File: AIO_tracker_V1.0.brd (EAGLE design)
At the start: 47 x 95 mm, 57 parts, among them J1 EDGE_ICSP, Q1 MOSFET-PCHANNELSMD, U2 USD-SOCKETNEW, X1 SMA-142-0701-881/886, Y2 16MHz

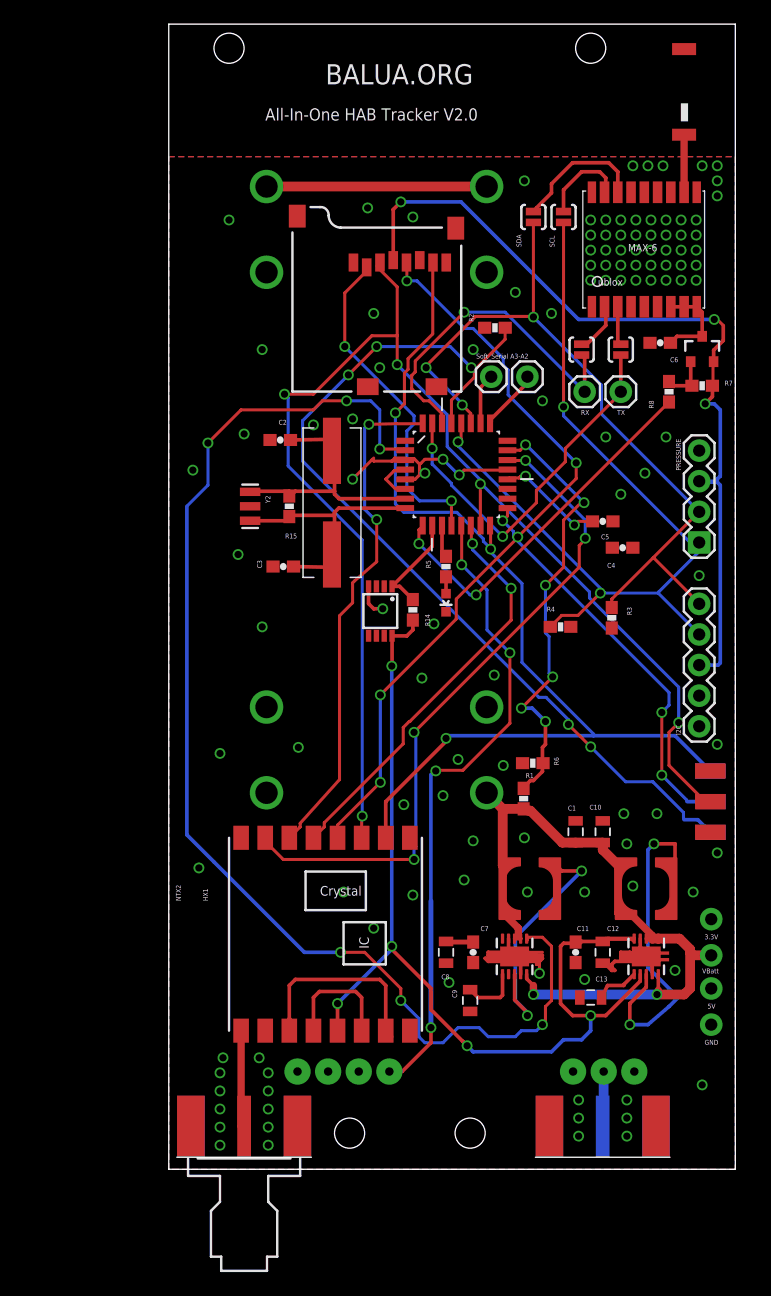
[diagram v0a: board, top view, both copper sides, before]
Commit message: added 9dof, new antena, new crystal, cutoff...
added 9dof, new antena, new crystal, cutoff system and changed layout
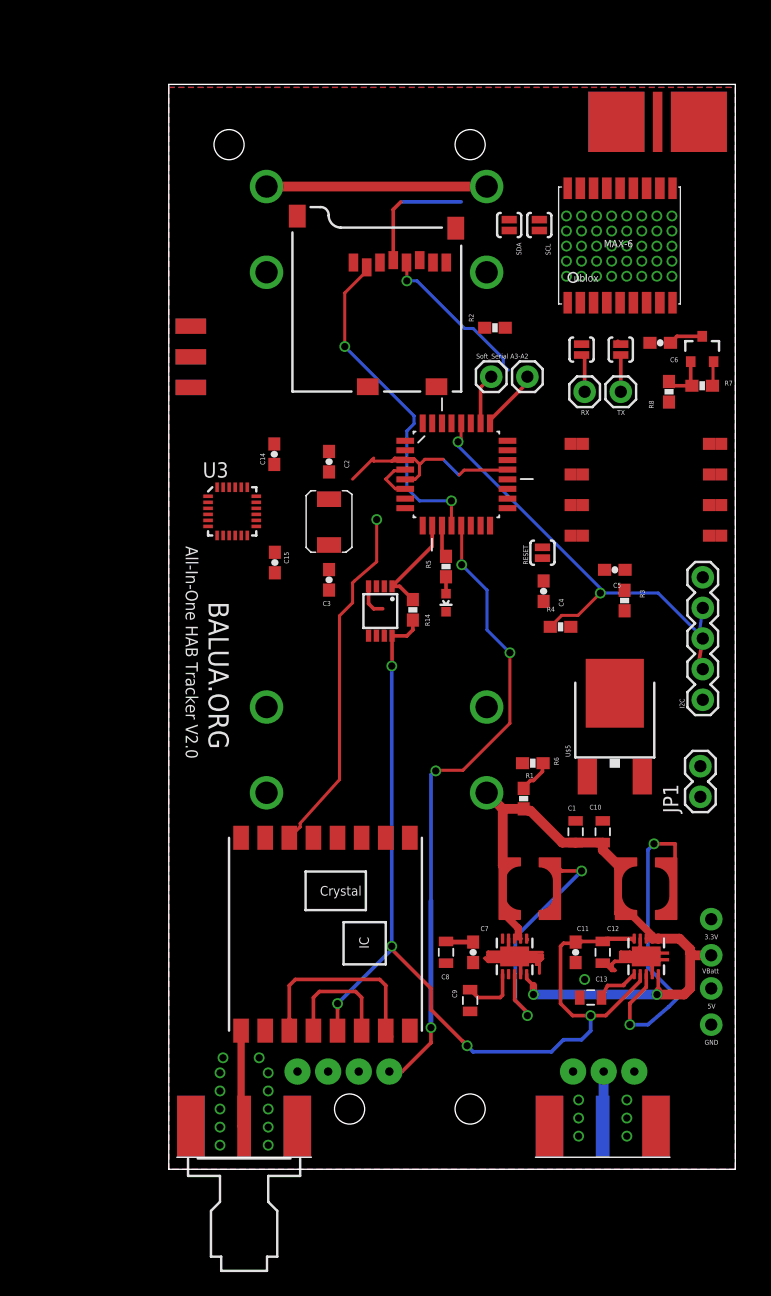
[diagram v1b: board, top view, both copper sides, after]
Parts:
- removed PRESSURE: (no value), SparkFun-Connectors:1X04
- removed R15: 1M, SparkFun-Passives:0603-RES
- removed Y2: 16MHz, SparkFun-FreqCtrl:RESONATOR-SMD
- added C14: 2.2nF, SparkFun-Passives:0603-CAP
- added C15: 0.1uF, SparkFun-Passives:0603-CAP
- added JP1: M02PTH, SparkFun-Connectors:1X02
- added SJ2: SOLDERJUMPERNO, SparkFun-Passives:SJ_2S-NO
- added TP1, TP10, TP11, TP12, TP13, TP14, TP15, TP16, TP2, TP3, TP4, TP5, TP6, TP7, TP8, TP9: TPTP10SQ, testpad:TP10SQ
- added U$5: LM2931_FIXED, SparkFun-PowerIC:DPAK
- added U3: (no value), SparkFun-Sensors:QFN-24-NP
- C2, C3: value 22pF -> 18pF
- U$2: value JTI_ANTENNA-1575AT43A40 -> JDGA-REMQV-ANTENNA; device Ava:JTI_ANTENNA-1575AT43A40 -> Ava:JDGA-RIGID_COMBO_PAD
- Y1: value (none) -> ABRACON_ABM3_CRYSTAL; device SparkFun-FreqCtrl:CRYSTAL-SMD-10.5X4.8-2PIN -> Ava:ABRACON_ABM3_CRYSTAL
- moved J1 56.7 mm to (0.83, 50.4)
- moved C4 7.48 mm to (30.1, 31.0), turned to 270 degrees
- moved C2 4.43 mm to (12.3, 41.7), turned to 270 degrees
- moved C5 4.14 mm to (36.0, 32.7)
- moved C3 3.96 mm to (12.3, 31.9), turned to 90 degrees
- moved U$2 3.04 mm to (39.6, 69.9), turned to 180 degrees
- moved I2C 2.22 mm to (43.3, 21.9)
- moved SJ1 2.12 mm to (27.2, 61.3)
- moved SJ3 2.12 mm to (29.7, 61.3)
- moved U$1 2.04 mm to (36.5, 59.8)
- moved R3 1.78 mm to (36.8, 30.2)
- moved Y1 0.18 mm to (12.4, 38.2)
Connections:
- removed net MARK: U1.24
- removed net SPACE: U1.19
- new net A6: U$7.15, U1.19
- new net CUTOUT: JP1.2, U$5.4
- new net GATE: U$5.1, U1.24
- new net N$14: TP13.TP, TP14.TP
- new net N$17: C15.1, U3.10
- new net N$18: C14.1, U3.20
- new net N$25: TP10.TP, TP11.TP, TP12.TP, TP9.TP
- new net N$8: C4.1, SJ2.1
- new net N$9: TP15.TP, TP16.TP
- net 3.3V: now also SJ2.2, TP3.TP, TP4.TP, U3.13, U3.3, U3.8; no longer C4.1, PRESSURE.3
- net A7: no longer U$7.15
- net GND: now also C14.2, C15.2, JP1.1, TP1.TP, TP2.TP, U$2.P$2, U$2.P$3, U$2.P$4, U$2.P$5, U3.1, U3.11, U3.15, U3.17, U3.18, U3.9; no longer PRESSURE.4, Y2.2
- net N$20: no longer R15.1, Y2.3
- net N$21: no longer R15.2, Y2.1
- net N$3: now also U$2.P$1; no longer U$2.FEED
- net SCL: now also TP7.TP, TP8.TP, U3.23; no longer PRESSURE.1
- net SDA: now also TP5.TP, TP6.TP, U3.24; no longer PRESSURE.2
- net VBATT: now also U$5.3
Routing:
- net MOSI: track 111.6 -> 0.00 mm, vias 5 -> 0
- net EN_POW_5V: track 103.9 -> 0.16 mm, vias 6 -> 0
- net MISO: track 85.4 -> 0.00 mm, vias 3 -> 0
- net SCK: track 96.2 -> 13.3 mm, vias 8 -> 1
- net RESET: track 77.8 -> 0.00 mm, vias 5 -> 0
- net SDA: track 63.0 -> 0.00 mm, vias 3 -> 0
- net 3.3V: track 162.8 -> 106.4 mm, vias 8 -> 5
- net A7: track 56.1 -> 0.00 mm, vias 4 -> 0
- net SCL: track 71.9 -> 36.5 mm, vias 3 -> 2
- net VBATTADC: track 37.3 -> 2.90 mm, vias 6 -> 0
- net RFM22_NSEL: track 34.1 -> 0.00 mm, vias 2 -> 0
- net GPSEN: track 30.8 -> 0.00 mm, vias 2 -> 0
- net UBLOX_RXD: track 30.9 -> 3.05 mm, vias 2 -> 0
- net UBLOX_TXD: track 28.2 -> 3.15 mm, vias 1 -> 0
- net N$21: track 21.8 -> 0.00 mm
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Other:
- board size 47 x 95 mm -> 47 x 90 mm
- board text added: "RESET"
- board text removed: "HX1"
- board text removed: "NTX2"

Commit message: size and placement defined
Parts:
- removed JP1: M02PTH, SparkFun-Connectors:1X02
- removed SJ2: SOLDERJUMPERNO, SparkFun-Passives:SJ_2S-NO
- added CUTOFF: M02PTH, SparkFun-Connectors:1X02
- 3.3V, 5V, GND, VBATT: value M01SMDNS -> M01PTH; device SparkFun-Connectors:1X01NS -> SparkFun-Connectors:1X01
- U$3: value RADIOMETRIX-HX1 -> NTX2-VERTICAL; device Ava:RADIOMETRIX-HX1 -> Ava:NTX2-VERTICAL
- moved TP12 49.2 mm to (-2.53, 29.9), flipped to the bottom, turned to 180 degrees
- moved TP16 48.1 mm to (-2.53, 32.5), flipped to the bottom, turned to 180 degrees
- moved TP9 47.5 mm to (-2.53, 35.0), flipped to the bottom, turned to 180 degrees
- moved TP13 47.4 mm to (-2.53, 37.5), flipped to the bottom, turned to 180 degrees
- moved TP11 47.2 mm to (-1.51, 29.9), flipped to the bottom, turned to 180 degrees
- moved TP15 46.1 mm to (-1.51, 32.5), flipped to the bottom, turned to 180 degrees
- moved TP10 45.4 mm to (-1.51, 35.0), flipped to the bottom, turned to 180 degrees
- moved TP14 45.4 mm to (-1.51, 37.5), flipped to the bottom, turned to 180 degrees
- moved BAT1 36.1 mm to (15.2, 4.77), turned to 0 degrees
- moved R2 33.8 mm to (-1.84, 33.7)
- moved SJ3 29.3 mm to (15.0, 36.0)
- moved U$2 29.1 mm to (36.0, 41.0)
- moved U2 28.6 mm to (5.96, 24.7)
- moved C6 28.5 mm to (38.1, 23.1), turned to 0 degrees
- moved U$1 28.3 mm to (32.9, 31.7)
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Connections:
- removed net N$8: C4.1, SJ2.1
- net 3.3V: now also C4.1; no longer SJ2.2
- net CUTOUT: now also CUTOFF.2; no longer JP1.2
- net GND: now also CUTOFF.1, U$3.RFGND1; no longer JP1.1, U$3.RFGND
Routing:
- net 3.3V: track 106.4 -> 0.00 mm, vias 5 -> 0
- net 5VEN: track 54.0 -> 0.00 mm, vias 4 -> 0
- net VBATT: track 59.8 -> 7.33 mm, vias 2 -> 0
- net GND: track 53.7 -> 1.41 mm, vias 59 -> 56
- net SCL: track 36.5 -> 0.00 mm, vias 2 -> 0
- net RFM22_NIRQ: track 29.5 -> 0.00 mm, vias 1 -> 0
- net SD_CS: track 27.9 -> 0.00 mm, vias 2 -> 0
- net N$19: track 27.9 -> 0.00 mm, vias 2 -> 0
- net N$7: track 20.8 -> 0.00 mm, vias 2 -> 0
- net N$10: track 18.3 -> 0.00 mm
- net N$29: track 16.8 -> 0.00 mm
- net SCK: track 13.3 -> 0.00 mm, vias 1 -> 0
- net N$30: track 10.3 -> 0.00 mm
- net TEMP: track 8.60 -> 0.00 mm
- net N$13: track 8.18 -> 0.00 mm
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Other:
- board size 47 x 90 mm -> 60 x 60 mm
- board text removed: "RESET"

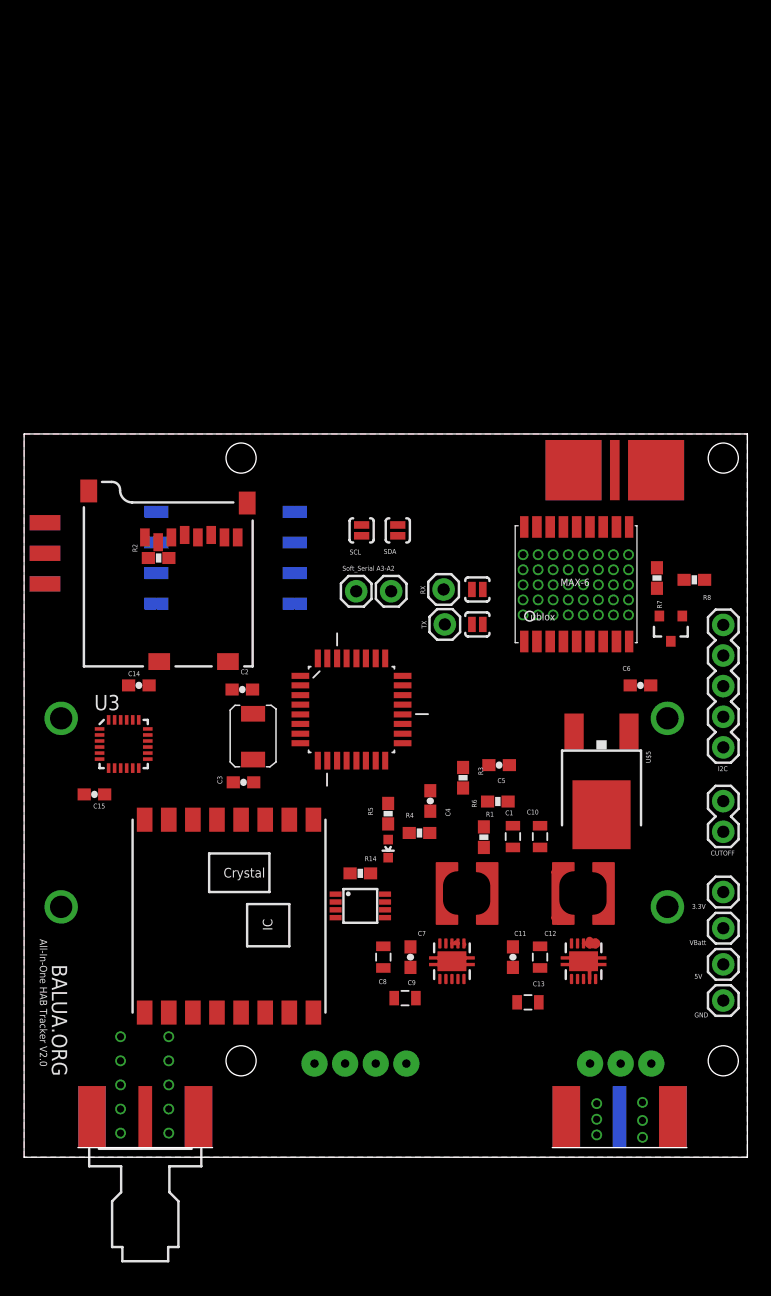
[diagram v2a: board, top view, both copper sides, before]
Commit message: tracker routed
tracker routed, some adjustments still in progress
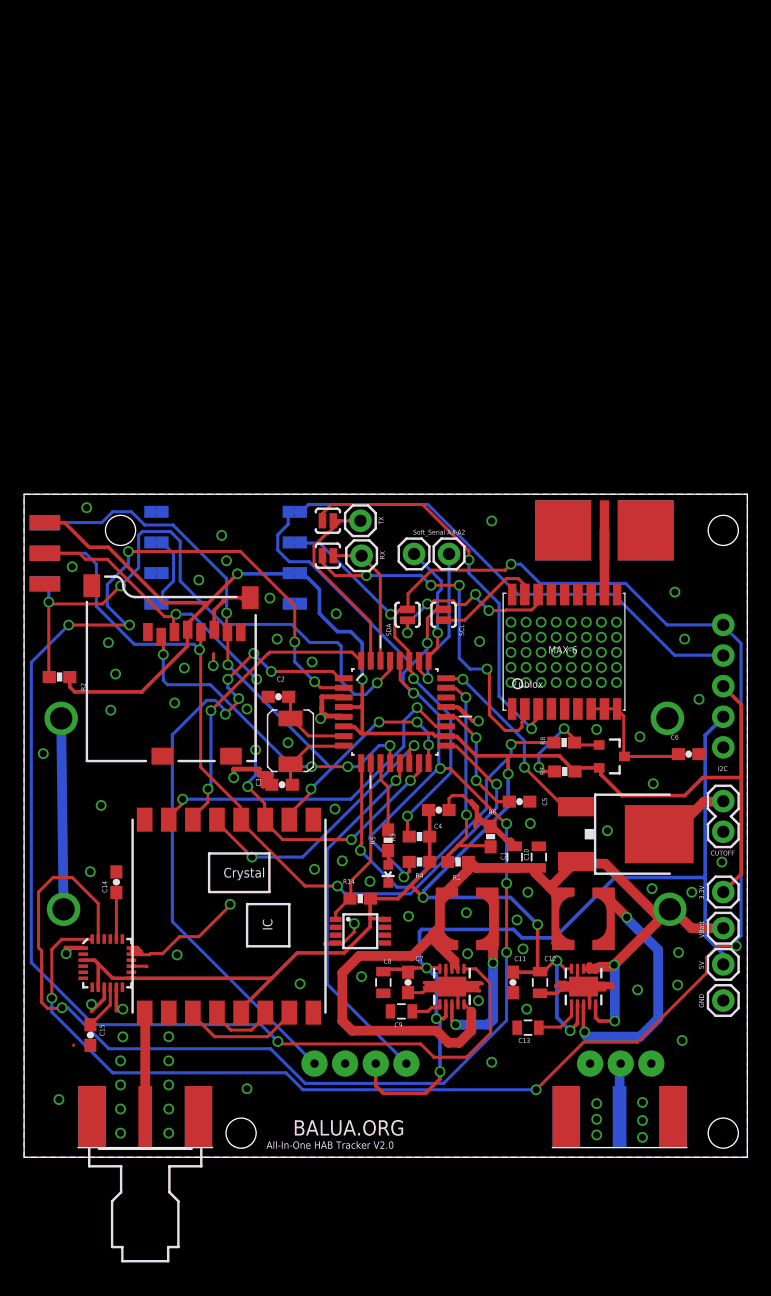
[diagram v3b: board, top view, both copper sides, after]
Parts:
- I2C: device SparkFun-Connectors:1X05 -> SparkFun-Connectors:1X05_NO_SILK
- moved C15 20.0 mm to (-7.50, -5.87), turned to 270 degrees
- moved U3 18.2 mm to (-6.10, 0.10)
- moved R7 17.8 mm to (31.9, 16.0), turned to 0 degrees
- moved R8 17.3 mm to (31.8, 18.4), turned to 0 degrees
- moved C14 16.4 mm to (-5.34, 6.82), turned to 90 degrees
- moved SJ5 15.1 mm to (12.2, 36.8), turned to 0 degrees
- moved R2 12.8 mm to (-10.1, 23.8), turned to 0 degrees
- moved SJ6 12.7 mm to (12.2, 33.9), turned to 0 degrees
- moved Q1 11.7 mm to (35.7, 17.2), turned to 270 degrees
- moved TX 11.1 mm to (14.9, 36.8), turned to 90 degrees
- moved SJ3 9.76 mm to (21.8, 29.0), turned to 270 degrees
- moved JP6 8.30 mm to (22.2, 34.0), turned to 180 degrees
- moved U2 7.85 mm to (6.21, 16.9)
- moved RX 7.35 mm to (15.0, 33.9), turned to 90 degrees
- moved SJ1 7.05 mm to (18.8, 29.0), turned to 270 degrees
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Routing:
- net 3.3V: track 0.00 -> 208.0 mm, vias 0 -> 7
- net SCL: track 0.00 -> 179.6 mm, vias 0 -> 8
- net SDA: track 0.00 -> 166.6 mm, vias 0 -> 7
- net EN_POW_5V: track 0.16 -> 116.5 mm, vias 0 -> 6
- net GND: track 1.41 -> 113.0 mm, vias 56 -> 119
- net VBATT: track 7.33 -> 88.0 mm, vias 0 -> 2
- net 5V: track 0.00 -> 76.0 mm, vias 0 -> 3
- net SCK: track 0.00 -> 69.5 mm, vias 0 -> 3
- net MISO: track 0.00 -> 55.3 mm, vias 0 -> 6
- net HX1: track 0.00 -> 53.5 mm, vias 0 -> 5
- net MOSI: track 0.00 -> 52.6 mm, vias 0 -> 6
- net RESET: track 0.00 -> 51.2 mm, vias 0 -> 3
- net N$11: track 0.20 -> 33.6 mm, vias 0 -> 2
- net GPSEN: track 0.00 -> 31.5 mm, vias 0 -> 2
- net N$12: track 0.00 -> 30.5 mm, vias 0 -> 4
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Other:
- board size 60 x 60 mm -> 60 x 55 mm

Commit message: final but without logo
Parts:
- 3.3V, 5V, GND, VBATT: value M01PTH -> M01SMDNS; device SparkFun-Connectors:1X01 -> SparkFun-Connectors:1X01NS
- CUTOFF: value M02PTH -> M021X02_NO_SILK; device SparkFun-Connectors:1X02 -> SparkFun-Connectors:1X02_NO_SILK
- moved 5V 3.00 mm to (45.0, -3.00)
- moved GND 3.00 mm to (45.0, 0.00)
- moved JP5 1.01 mm to (18.4, 34.4)
- moved JP6 1.01 mm to (21.3, 34.4)
- moved C4 0.72 mm to (21.0, 13.4)
- moved R6 0.51 mm to (25.6, 10.1)
- moved C2 0.30 mm to (8.40, 22.2)
- moved C9 0.20 mm to (18.3, -4.10)
- moved C8 0.20 mm to (16.6, -1.50)
- moved BAT2 0.17 mm to (15.4, 20.4)
- moved C7 0.10 mm to (18.9, -1.60)
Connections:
- new net N$9: TP11.TP, TP12.TP
- net N$25: no longer TP11.TP, TP12.TP
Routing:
- net SDA: track 166.6 -> 188.5 mm
- net GND: track 113.0 -> 92.0 mm, vias 119 -> 117
- net RESET: track 51.2 -> 43.7 mm
- net N$25: track 7.88 -> 1.02 mm
- net MOSI: track 52.6 -> 55.9 mm
- net 5V: track 76.0 -> 78.0 mm
- net 3.3V: track 208.0 -> 210.0 mm
- net VBATTADC: track 19.3 -> 20.9 mm
- net A2: track 10.2 -> 11.6 mm
- net N$9: track 0.00 -> 1.02 mm
- net N$12: track 30.5 -> 31.4 mm
- net VBATT: track 88.0 -> 88.9 mm
- net HX1: track 53.5 -> 54.3 mm
- net A3: track 12.9 -> 13.6 mm

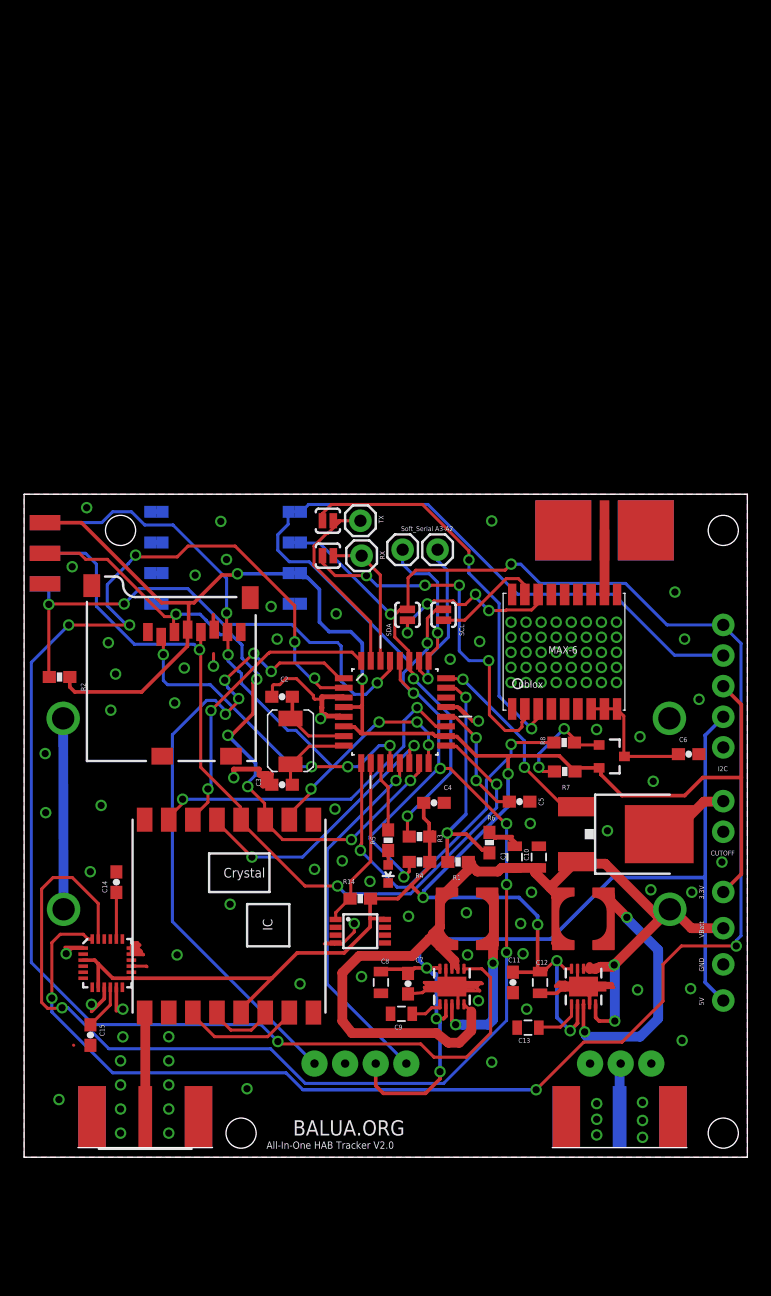
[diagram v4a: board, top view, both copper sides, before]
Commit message: corrected pcb errors for oshpark
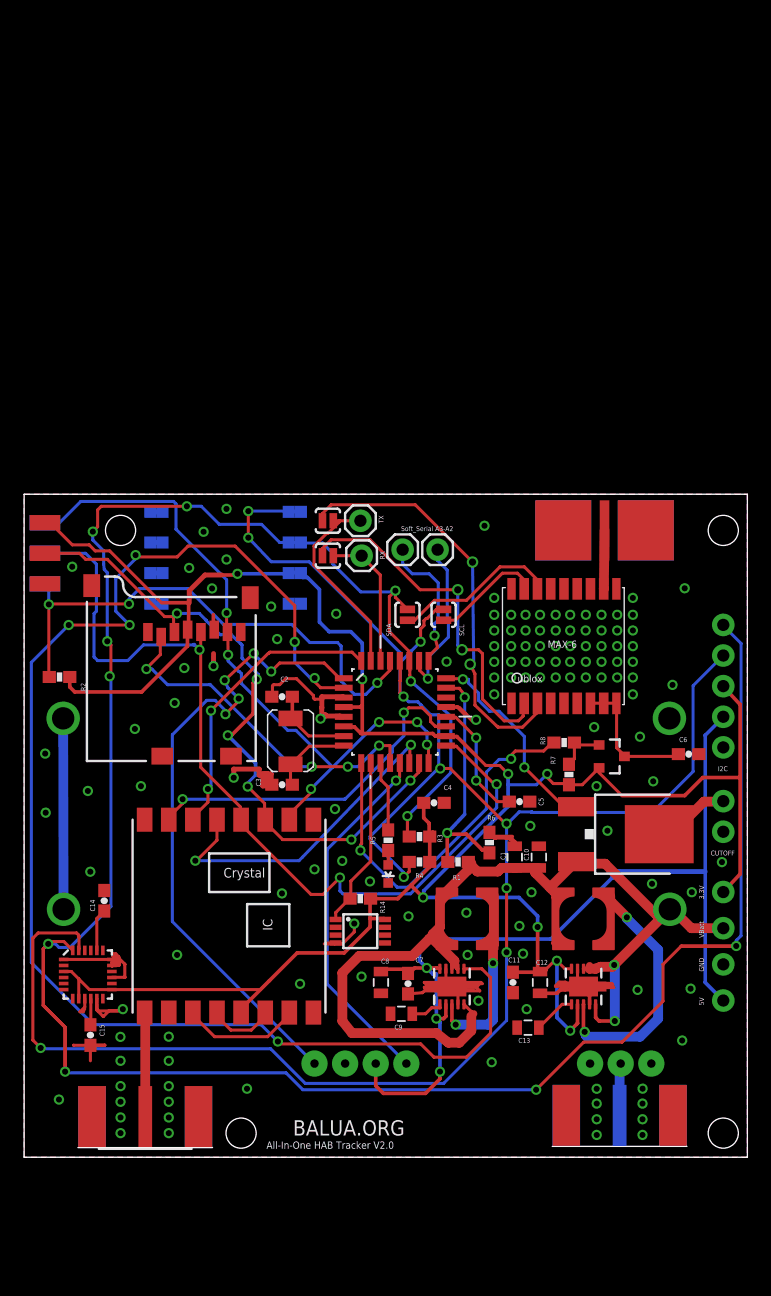
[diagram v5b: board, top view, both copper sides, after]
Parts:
- moved U3 1.87 mm to (-7.72, -0.84)
- moved C14 1.84 mm to (-6.35, 5.28)
- moved U$1 0.47 mm to (31.8, 26.6)
- moved R7 0.43 mm to (32.2, 15.8), turned to 270 degrees
- moved X1 0.10 mm to (36.4, -15.1)
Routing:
- net SDA: track 188.5 -> 219.2 mm, vias 7 -> 11
- net SCL: track 179.3 -> 168.8 mm, vias 8 -> 10
- net GND: track 92.0 -> 100.5 mm, vias 117 -> 132
- net SCK: track 69.5 -> 75.5 mm
- net N$2: track 9.83 -> 4.52 mm, vias 2 -> 0
- net RFM22_NSEL: track 23.2 -> 27.8 mm
- net 3.3V: track 210.0 -> 212.2 mm, vias 7 -> 8
- net MISO: track 55.7 -> 57.6 mm
- net SD_CS: track 27.7 -> 29.5 mm
- net N$15: track 15.6 -> 13.8 mm, vias 4 -> 0
- net N$17: track 3.80 -> 2.19 mm
- net N$11: track 33.6 -> 35.2 mm
- net N$12: track 31.4 -> 30.0 mm, vias 4 -> 2
- net GATE: track 16.5 -> 17.2 mm
- net N$6: track 10.9 -> 11.5 mm
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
